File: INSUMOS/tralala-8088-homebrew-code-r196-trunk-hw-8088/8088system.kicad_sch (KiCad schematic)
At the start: 20 parts, among them P10 Conn_01x10, P11 ~{TEST}, P2 NMI, P3 LA1034 Logicport Connection, P4 Conn_01x05_Female, U1 74HCT00, U10 74HCT373, U11 AS6C4008, U12 SST39SF040, U13 74HCT138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

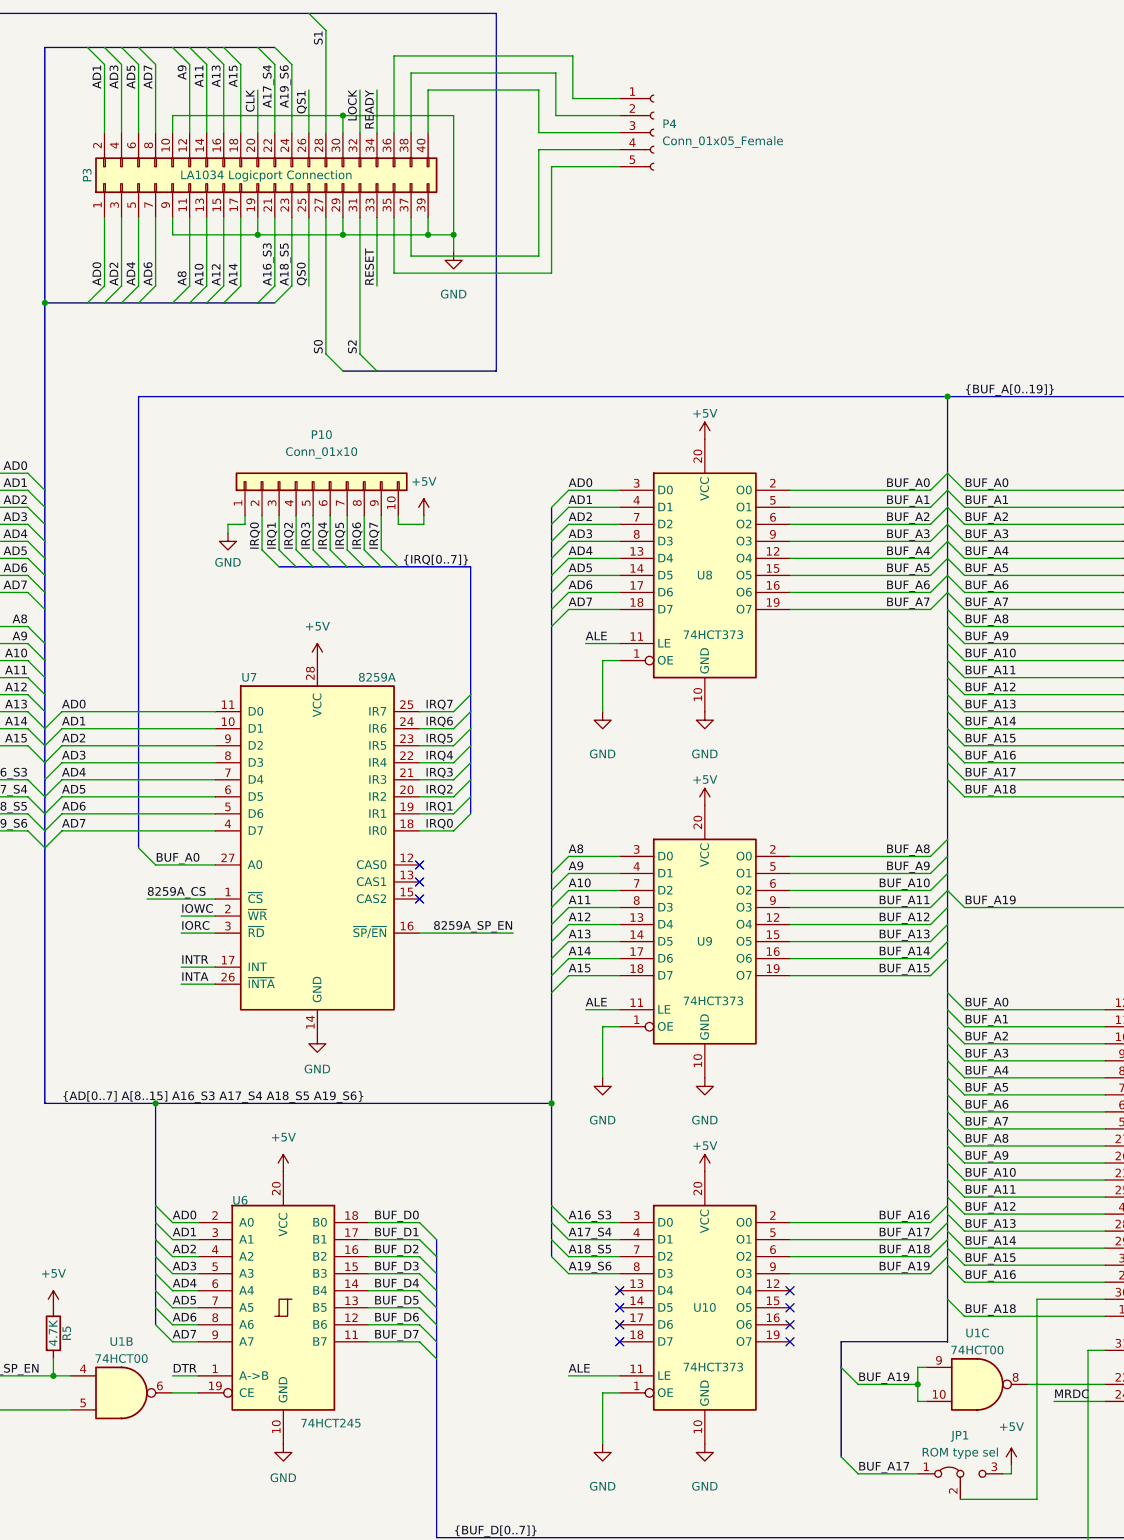
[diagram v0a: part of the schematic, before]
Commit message: Inicio da bios apos testes
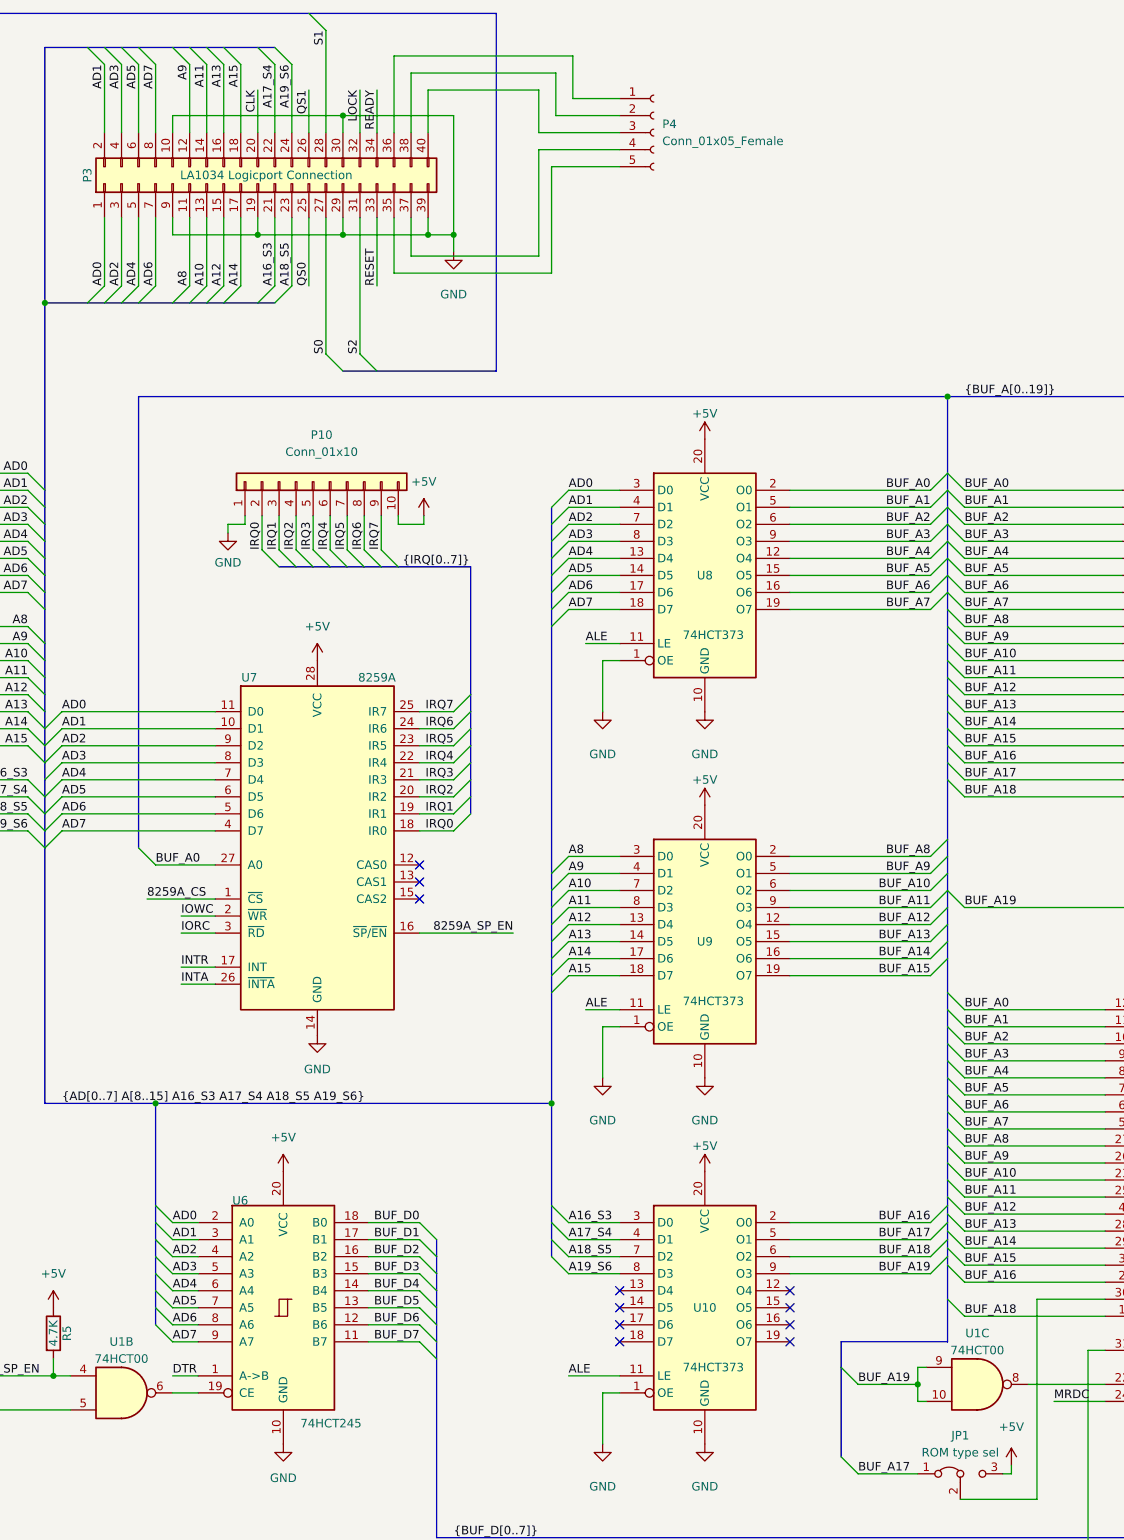
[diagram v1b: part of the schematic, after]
